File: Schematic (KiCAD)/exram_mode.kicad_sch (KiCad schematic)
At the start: 95 parts

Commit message: - Lots of additional comments and signal name improvements.  - "Don't know what this is yet but it is important" section of the pulse channels:    - I worked out the logic and it is a 4-bit binary up-counter with preload, made from gates and D-latches instead of T-flip-flops.    - It is extremely similar to the envelope counter, but takes twice the die space and much more traces.    - None of its outputs go anywhere else, so I believe that it has no actual function.    - It seems to be a previous attempt at making the envelope counter and it got disconnected and left in.    - Each pulse channel has its own copy and I moved both of them to the "Artifacts" sheet.    - The wasted space amounts to about half of one of the large columns on the left side of the die.  - A couple of "OAI2" cells that noted "unclear order": I determined the correct order of the inputs based on several others which were known.  - Deduced the purpose of the 2 separate methods of scanline detection:    - The one looking for 3 consecutive reads finds the start of a scanline.    - The one counting PPU /RD to find PPU cycle 336, finds the end of the scanline.    - I moved these beside each other on the same sheet for clarity.  - A66.5 Changed from Nand to Nor in order to make sense.  - Basic test mode:    - Pin 92: Active low, enables test mode.    - Pin 29: In test mode, it gives external control of "Scanline Start Detection", which is normally done with the familiar 3 matching PPU reads.  When not in test mode, the pin has no function.    - Pin 30: In test mode, it gives external control of "Scanline End Detection", which is normally done by counting PPU /RD to find PPU cycle 336.  It also gives control of "Pulse Length Clock" when in test mode.  When not in test mode, the pin has no function.    - Pin 98/SL3: In test mode, it gives external control of "Pulse Timer Clock".  Whether or not in test mode, this pin low makes the MMC5 pretend $5104 had not yet been written since reset, probably as a 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
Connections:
- net SL3_PIN is gone; now on net /SL3_PIN_98{PinInv}: BN1. (X)
- net at BL100. (X): now also BL101. (X); no longer BL99. (/Q)
- net /SL3_PIN_98{PinInv}: now reaches BN1. (X)
- net /SL3_PIN_98{PinInv}: no longer BL98. (/Q)
- net at BL90. (X): now also BL91. (X); no longer BL89. (/Q)
- net V-Split_Rendering{N15}: now reaches BK92. (X)
- net V-Split_Rendering{N15}: now also BK94. (X); no longer BK93. (X)
- net at BL93. (X): now also BL92. (X); no longer BN2. (X)
- net at BJ10. (X): now also BJ11. (/Q7); no longer BJ9. (X)
- net at BL88. (X): now also BL86. (X); no longer BL84. (X)
- net at BL92. (X): now also BL94. (X); no longer BL93. (X)
- net at BM9. (X): now also BM10. (X); no longer BM8. (X)
- net at BM10. (X): now also BL91. (X); no longer BM9. (X)
- net at BL84. (X): now also BL85. (X); no longer BL87. (X)
- net at BL103. (X): now also BJ39b. (X); no longer BL95. (X)
- net at BL85. (X): now also BL86. (X); no longer BL82. (X)
- net at BM3. (X): now also BM4. (X); no longer BM2. (X)
- net at BM4. (X): now also BM5. (X); no longer BM3. (X)
- net at BL106. (X): now also BL109. (/Q); no longer BL105. (X)
- removed net V-Split_Side_Latched{N15}: BK92. (X), BK94. (X)
- new net: BL81. (X), BL87. (X)
- new net: BJ40. (Q9), BK78. (Q7), BK89. (X)
- new net: BK84. (X), BL102. (X), BL105. (X), BL107. (X), BN3. (X), BN4. (X)
- new net: BK83. (X), BK84. (X)
- new net: BK84. (X), BK86. (X)
- new net: BL102. (X), BL99. (/Q)
- new net: BL108. (X), BL99. (/Q)
- new net: BL100. (X), BL99. (/Q)
- new net: BL93. (X), BL94. (X), BL98. (/Q)
- new net: BL98. (/Q), BN1. (X)
- new net: BJ40. (Q9), BJ43. (X)
- new net: BK91. (X), BK93. (X)
- new net: BK77. (Q7), BK90. (X)
- new net: BK77. (Q7), BK78. (Q7) (x8)
- new net: BK79. (X), BK81. (X), BK82. (Q1)
- new net: BL89. (/Q), BL90. (X)
- new net: BK92. (X), BK93. (X)
- new net: BL93. (X), BN2. (X)
- new net: BJ7. (X), BJ9. (X)
- new net: BJ10. (X), BJ9. (X)
- new net: BJ32. (X), BJ33. (X), BJ34. (X), BJ35. (X), BJ36. (X), BJ37. (X), BJ38. (X), BJ39. (X), BJ39b. (X) (x2)
- new net: BL84. (X), BL88. (X)
- new net: BL88. (X), BM5. (X), BM6. (X)
- new net: BM8. (X), BM9. (X)
- new net: BK79. (X), BK82. (Q1), BL96. (X)
- new net: BL84. (X), BL87. (X)
- new net: BL104. (X), BL95. (X)
- new net: BL103. (X), BL95. (X)
- new net: BL82. (X), BL85. (X)
- new net: BL83. (X), BL84. (X)
- new net: BJ51. (X), BK96. (X)
- new net: BM2. (X), BM3. (X)
- new net: BK80. (X), BK82. (Q1)
- new net: BL105. (X), BL106. (X)
- new net: BL91. (X), BL92. (X)
- new net: BJ40. (Q9), BJ50. (X)
- new net: BJ40. (Q9), BJ46. (X)
- new net: BJ40. (Q9), BJ42. (X)
- new net: BJ40. (Q9), BJ44. (X)
- new net: BJ40. (Q9), BJ49. (X)
- new net: BJ40. (Q9), BJ45. (X)
- new net: BJ40. (Q9), BJ48. (X)
- new net: BJ40. (Q9), BJ47. (X)
- new net: BJ40. (Q9), BJ41. (X)
- new net: BK94. (X), BK95. (X)
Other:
- note added: "Consider: ExRAM NEVER contains pattern tables and that should be related to how PPU /A13 is being used here."
- note added: "Question: Why should we care about PPU /A13 AT ALL when the CPU has control of ExRAM address bus? Consider: ExRAM can still be used as a nametable when ExRAM mode is set to CPU mode."
- note added: "TRUE when: ExRAM is mode $1x, which gives CPU access but no PPU access, *OR* PPU is accessing NT or AT"
- note added: "That doesn't make sense because what if you have a nametable assigned to ExRAM in $5105? It needs ExRAM Ax coming from PPU. Signal A9 (+ExRAM Nametable Access) is VERY closeby but no obvious connection"
- note added: "This is the write signal for the ExRAM itself."
- note added: "Writing to ExRAM via $5C00-5FFF in mode %10"
- note added: "Writing to an ExRAM nametable via PPU via $2000"
- moved on the sheet: BJ40, BJ41, BJ42, BJ43, BJ44, BJ45, BJ46, BJ47, BJ48, BJ49, BJ50, BJ51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

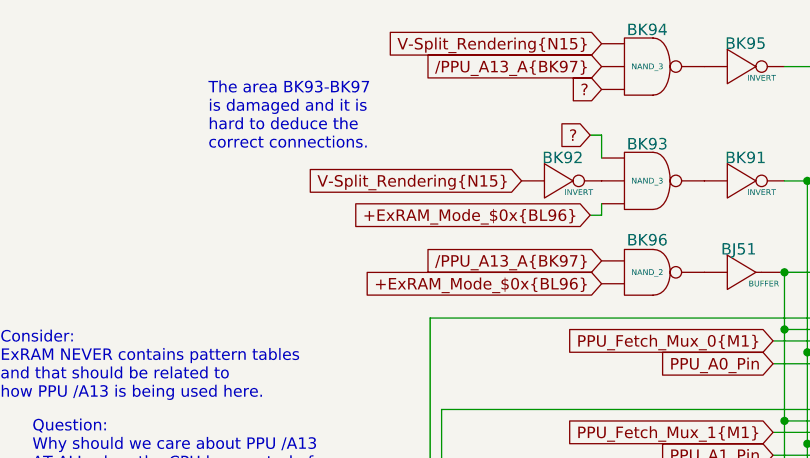
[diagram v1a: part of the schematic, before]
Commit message: - I have fixed all of the problems I was having in the $2006 section, and things are all going places that make sense now.  - I am making good progress on the timer as well.  - I pulled a couple changes back into the letterless SVG and updated the schematic.
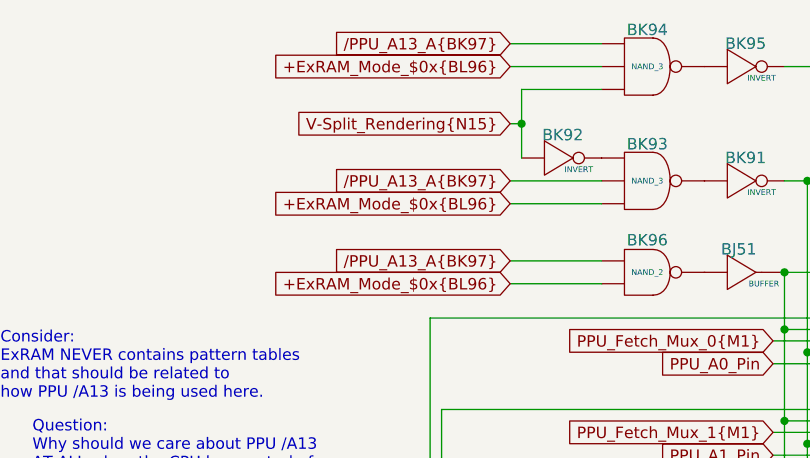
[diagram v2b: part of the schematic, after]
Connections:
- net +ExRAM_Mode_$0x{BL96}: now also BK94. (X)
- net ?: no longer BK93. (X), BK94. (X)
- net /PPU_A13_A{BK97}: now also BK93. (X)
- net at BL100. (X): now also BL101. (X); no longer BL99. (/Q)
- net at BL90. (X): now also BL91. (X); no longer BL89. (/Q)
- net at BL93. (X): now also BL92. (X); no longer BN2. (X)
- net at BJ10. (X): now also BJ11. (/Q7); no longer BJ9. (X)
- net at BL88. (X): now also BL86. (X); no longer BL84. (X)
- net at BL92. (X): now also BL94. (X); no longer BL93. (X)
- net at BM9. (X): now also BM10. (X); no longer BM8. (X)
- net at BM10. (X): now also BL91. (X); no longer BM9. (X)
- net at BL84. (X): now also BL85. (X); no longer BL87. (X)
- net at BL103. (X): now also BJ39b. (X); no longer BL95. (X)
- net at BL85. (X): now also BL86. (X); no longer BL82. (X)
- net at BM3. (X): now also BM4. (X); no longer BM2. (X)
- net at BM4. (X): now also BM5. (X); no longer BM3. (X)
- net at BL106. (X): now also BL109. (/Q); no longer BL105. (X)
- new net: BL81. (X), BL87. (X)
- new net: BJ40. (Q9), BK78. (Q7), BK89. (X)
- new net: BK84. (X), BL102. (X), BL105. (X), BL107. (X), BN3. (X), BN4. (X)
- new net: BK83. (X), BK84. (X)
- new net: BK84. (X), BK86. (X)
- new net: BL102. (X), BL99. (/Q)
- new net: BL108. (X), BL99. (/Q)
- new net: BL100. (X), BL99. (/Q)
- new net: BL93. (X), BL94. (X), BL98. (/Q)
- new net: BL98. (/Q), BN1. (X)
- new net: BJ40. (Q9), BJ43. (X)
- new net: BK91. (X), BK93. (X)
- new net: BK77. (Q7), BK90. (X)
- new net: BK77. (Q7), BK78. (Q7) (x8)
- new net: BK79. (X), BK81. (X), BK82. (Q1)
- new net: BL89. (/Q), BL90. (X)
- new net: BK92. (X), BK93. (X)
- new net: BL93. (X), BN2. (X)
- new net: BJ7. (X), BJ9. (X)
- new net: BJ10. (X), BJ9. (X)
- new net: BJ32. (X), BJ33. (X), BJ34. (X), BJ35. (X), BJ36. (X), BJ37. (X), BJ38. (X), BJ39. (X), BJ39b. (X) (x2)
- new net: BL84. (X), BL88. (X)
- new net: BL88. (X), BM5. (X), BM6. (X)
- new net: BM8. (X), BM9. (X)
- new net: BK79. (X), BK82. (Q1), BL96. (X)
- new net: BL84. (X), BL87. (X)
- new net: BL104. (X), BL95. (X)
- new net: BL103. (X), BL95. (X)
- new net: BL82. (X), BL85. (X)
- new net: BL83. (X), BL84. (X)
- new net: BJ51. (X), BK96. (X)
- new net: BM2. (X), BM3. (X)
- new net: BK80. (X), BK82. (Q1)
- new net: BL105. (X), BL106. (X)
- new net: BL91. (X), BL92. (X)
- new net: BJ40. (Q9), BJ50. (X)
- new net: BJ40. (Q9), BJ46. (X)
- new net: BJ40. (Q9), BJ42. (X)
- new net: BJ40. (Q9), BJ44. (X)
- new net: BJ40. (Q9), BJ49. (X)
- new net: BJ40. (Q9), BJ45. (X)
- new net: BJ40. (Q9), BJ48. (X)
- new net: BJ40. (Q9), BJ47. (X)
- new net: BJ40. (Q9), BJ41. (X)
- new net: BK94. (X), BK95. (X)
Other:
- note removed: "The area BK93-BK97 is damaged and it is hard to deduce the correct connections."
- moved on the sheet: BK92
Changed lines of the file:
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@@
 		)
 	)
-	(text "The area BK93-BK97\nis damaged and it is\nhard to deduce the\ncorrect connections."
-		(exclude_from_sim no)
-		(at 236.982 27.178 0)
-		(effects
-			(font
-				(size 1.27 1.27)
-			)
-			(justify left)
-		)
-	)
 	(text "Writing to ExRAM\nvia $5C00-5FFF\nin mode %10"
 		(exclude_from_sim no)
@@
 	)
 	(junction
+		(at 271.78 27.94)
+		(diameter 0)
+		(color 0 0 0 0)
+	)
+	(junction
 		(at 118.11 76.2)
 		(diameter 0)
@@
 	(wire
 		(pts
+			(xy 270.51 34.29) (xy 280.67 34.29)
+		)
+		(stroke
+			(width 0)
+			(type default)
+		)
+	)
+	(wire
+		(pts
 			(xy 86.36 33.02) (xy 78.74 33.02)
 		)
@@
 	(wire
 		(pts
+			(xy 270.51 43.18) (xy 280.67 43.18)
+		)
+		(stroke
+			(width 0)
+			(type default)
+		)
+	)
+	(wire
+		(pts
 			(xy 66.04 82.55) (xy 66.04 91.44)
 		)
@@
 	(wire
 		(pts
-			(xy 280.67 38.1) (xy 279.4 38.1)
-		)
-		(stroke
-			(width 0)
-			(type default)
-		)
-	)
-	(wire
-		(pts
 			(xy 54.61 222.25) (xy 53.34 222.25)
 		)
@@
 	(wire
 		(pts
-			(xy 279.4 29.21) (xy 280.67 29.21)
-		)
-		(stroke
-			(width 0)
-			(type default)
-		)
-	)
-	(wire
-		(pts
 			(xy 299.72 85.09) (xy 308.61 85.09)
 		)
@@
 	(wire
 		(pts
+			(xy 270.51 21.59) (xy 280.67 21.59)
+		)
+		(stroke
+			(width 0)
+			(type default)
+		)
+	)
+	(wire
+		(pts
 			(xy 303.53 104.14) (xy 303.53 93.98)
 		)
@@
 	(wire
 		(pts
+			(xy 270.51 45.72) (xy 280.67 45.72)
+		)
+		(stroke
+			(width 0)
+			(type default)
+		)
+	)
+	(wire
+		(pts
 			(xy 113.03 124.46) (xy 113.03 132.08)
 		)
@@
 	(wire
 		(pts
+			(xy 270.51 19.05) (xy 280.67 19.05)
+		)
+		(stroke
+			(width 0)
+			(type default)
+		)
+	)
+	(wire
+		(pts
 			(xy 303.53 73.66) (xy 303.53 63.5)
 		)
@@
 	(wire
 		(pts
+			(xy 271.78 27.94) (xy 271.78 24.13)
+		)
+		(stroke
+			(width 0)
+			(type default)
+		)
+	)
+	(wire
+		(pts
 			(xy 128.27 167.64) (xy 128.27 182.88)
 		)
@@
 	(wire
 		(pts
-			(xy 280.67 36.83) (xy 280.67 38.1)
+			(xy 270.51 36.83) (xy 280.67 36.83)
 		)
 		(stroke
@@
 	(wire
 		(pts
-			(xy 118.11 76.2) (xy 127 76.2)
+			(xy 270.51 27.94) (xy 271.78 27.94)
 		)
 		(stroke
@@
 	(wire
 		(pts
-			(xy 100.33 168.91) (xy 97.79 168.91)
+			(xy 118.11 76.2) (xy 127 76.2)
 		)
 		(stroke
@@
 	(wire
 		(pts
-			(xy 243.84 143.51) (xy 243.84 153.67)
+			(xy 100.33 168.91) (xy 97.79 168.91)
 		)
 		(stroke
@@
 	(wire
 		(pts
-			(xy 77.47 81.28) (xy 77.47 83.82)
+			(xy 243.84 143.51) (xy 243.84 153.67)
 		)
 		(stroke
@@
 	(wire
 		(pts
-			(xy 300.99 60.96) (xy 308.61 60.96)
+			(xy 77.47 81.28) (xy 77.47 83.82)
 		)
 		(stroke
@@
 	(wire
 		(pts
-			(xy 262.89 120.65) (xy 260.35 120.65)
+			(xy 300.99 60.96) (xy 308.61 60.96)
 		)
 		(stroke
@@
 	(wire
 		(pts
-			(xy 303.53 134.62) (xy 303.53 124.46)
+			(xy 262.89 120.65) (xy 260.35 120.65)
 		)
 		(stroke
@@
 	(wire
 		(pts
-			(xy 269.24 133.35) (xy 260.35 133.35)
+			(xy 303.53 134.62) (xy 303.53 124.46)
 		)
 		(stroke
@@
 	(wire
 		(pts
-			(xy 280.67 29.21) (xy 280.67 31.75)
+			(xy 269.24 133.35) (xy 260.35 133.35)
 		)
 		(stroke
@@
 	(wire
 		(pts
+			(xy 271.78 27.94) (xy 271.78 31.75)
+		)
+		(stroke
+			(width 0)
+			(type default)
+		)
+	)
+	(wire
+		(pts
 			(xy 271.78 130.81) (xy 271.78 138.43)
 		)
@@
 	(wire
 		(pts
+			(xy 271.78 24.13) (xy 280.67 24.13)
+		)
+		(stroke
+			(width 0)
+			(type default)
+		)
+	)
+	(wire
+		(pts
 			(xy 264.16 123.19) (xy 260.35 123.19)
 		)
@@
 	(global_label "+ExRAM_Mode_$0x{BL96}"
 		(shape input)
-		(at 279.4 38.1 180)
+		(at 270.51 36.83 180)
 		(fields_autoplaced yes)
 		(effects
@@
 		)
 		(property "Intersheetrefs" "${INTERSHEET_REFS}"
-			(at 252.2245 38.1 0)
+			(at 243.3345 36.83 0)
 			(effects
 				(font
@@
 	(global_label "{slash}PPU_A13_A{BK97}"
 		(shape input)
-		(at 280.67 21.59 180)
+		(at 270.51 34.29 180)
+		(fields_autoplaced yes)
+		(effects
+			(font
+				(size 1.27 1.27)
+			)
+			(justify right)
+		)
+		(property "Intersheetrefs" "${INTERSHEET_REFS}"
+			(at 249.14 34.29 0)
+			(effects
+				(font
+					(size 1.27 1.27)
+				)
+				(justify right)
+				(hide yes)
+			)
+		)
+	)
+	(global_label "{slash}PPU_A13_A{BK97}"
+		(shape input)
+		(at 270.51 19.05 180)
 		(fields_autoplaced yes)
 		(effects
@@
 		)
 		(property "Intersheetrefs" "${INTERSHEET_REFS}"
-			(at 259.3 21.59 0)
+			(at 249.14 19.05 0)
 			(effects
 				(font
@@
 	(global_label "+ExRAM_Mode_$0x{BL96}"
 		(shape input)
+		(at 270.51 21.59 180)
+		(fields_autoplaced yes)
+		(effects
+			(font
+				(size 1.27 1.27)
+			)
+			(justify right)
+		)
+		(property "Intersheetrefs" "${INTERSHEET_REFS}"
+			(at 243.3345 21.59 0)
+			(effects
+				(font
+					(size 1.27 1.27)
+				)
+				(justify right)
+				(hide yes)
+			)
+		)
+	)
+	(global_label "+ExRAM_Mode_$0x{BL96}"
+		(shape input)
 		(at 219.71 203.2 180)
 		(fields_autoplaced yes)
@@
 		)
 	)
-	(global_label "V-Split_Rendering{N15}"
-		(shape input)
-		(at 280.67 19.05 180)
-		(fields_autoplaced yes)
-		(effects
-			(font
-				(size 1.27 1.27)
-			)
-			(justify right)
-		)
-		(property "Intersheetrefs" "${INTERSHEET_REFS}"
-			(at 254.8249 19.05 0)
-			(effects
-				(font
-					(size 1.27 1.27)
-				)
-				(justify right)
-				(hide yes)
-			)
-		)
-	)
 	(global_label "+PPU_RD_A{BJ8}"
 		(shape input)
@@
 	(global_label "+ExRAM_Mode_$0x{BL96}"
 		(shape input)
-		(at 280.67 45.72 180)
+		(at 270.51 45.72 180)
 		(fields_autoplaced yes)
 		(effects
@@
 		)
 		(property "Intersheetrefs" "${INTERSHEET_REFS}"
-			(at 253.4945 45.72 0)
+			(at 243.3345 45.72 0)
 			(effects
 				(font
@@
 		)
 	)
-	(global_label "?"
-		(shape input)
-		(at 279.4 29.21 180)
-		(fields_autoplaced yes)
-		(effects
-			(font
-				(size 1.27 1.27)
-			)
-			(justify right)
-		)
-		(property "Intersheetrefs" "${INTERSHEET_REFS}"
-			(at 275.3262 29.21 0)
-			(effects
-				(font
-					(size 1.27 1.27)
-				)
-				(justify right)
-				(hide yes)
-			)
-		)
-	)
 	(global_label "{slash}CPU_Write_To_ExRAM_Any_Mode{BK85}"
 		(shape input)
@@
 	(global_label "V-Split_Rendering{N15}"
 		(shape input)
-		(at 271.78 34.29 180)
+		(at 270.51 27.94 180)
 		(fields_autoplaced yes)
 		(effects
@@
 		)
 		(property "Intersheetrefs" "${INTERSHEET_REFS}"
-			(at 245.9349 34.29 0)
+			(at 244.6649 27.94 0)
 			(effects
 				(font
@@
 		)
 	)
-	(global_label "?"
-		(shape input)
-		(at 280.67 24.13 180)
-		(fields_autoplaced yes)
-		(effects
-			(font
-				(size 1.27 1.27)
-			)
-			(justify right)
-		)
-		(property "Intersheetrefs" "${INTERSHEET_REFS}"
-			(at 276.5962 24.13 0)
-			(effects
-				(font
-					(size 1.27 1.27)
-				)
-				(justify right)
-				(hide yes)
-			)
-		)
-	)
 	(global_label "ExRAM_D2_Read"
 		(shape input)
@@
 	(global_label "{slash}PPU_A13_A{BK97}"
 		(shape input)
-		(at 280.67 43.18 180)
+		(at 270.51 43.18 180)
 		(fields_autoplaced yes)
 		(effects
@@
 		)
 		(property "Intersheetrefs" "${INTERSHEET_REFS}"
-			(at 259.3 43.18 0)
+			(at 249.14 43.18 0)
 			(effects
 				(font
@@
 		(lib_name "INVERT_11")
 		(lib_id "MMC5:INVERT")
-		(at 276.86 34.29 0)
+		(at 276.86 31.75 0)
 		(unit 1)
 		(exclude_from_sim no)
@@
 		(fields_autoplaced yes)
 		(property "Reference" "BK92"
-			(at 276.352 30.988 0)
+			(at 276.352 28.448 0)
 			(do_not_autoplace yes)
 			(effects
@@
 		)
 		(property "Value" "INVERT"
-			(at 278.13 35.56 0)
+			(at 278.13 33.02 0)
 			(do_not_autoplace yes)
 			(effects
@@
 		)
 		(property "Footprint" ""
-			(at 276.86 34.29 0)
+			(at 276.86 31.75 0)
 			(effects
 				(font
@@
 		)
 		(property "Datasheet" ""
-			(at 276.86 34.29 0)
+			(at 276.86 31.75 0)
 			(effects
 				(font
@@
 		)
 		(property "Description" ""
-			(at 276.86 34.29 0)
+			(at 276.86 31.75 0)
 			(effects
 				(font

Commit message: Schematic and SVG Updates
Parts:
- removed BN1: INVERT, symbol MMC5:INVERT
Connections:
- net ? is gone; now on net /Q{BL109}: BL109. (/Q)
- net Q{BL109} is gone; now on net /Q{BL109}: BK89. (X), BL108. (X), BL109. (/Q)
- net /Q{BL109}: now reaches BL108. (X)
- net /Q{BL109}: no longer BL99. (/Q)
- net at BL100. (X): now also BL101. (X); no longer BL99. (/Q)
- net at BL90. (X): now also BL91. (X); no longer BL89. (/Q)
- net at BL93. (X): now also BL92. (X); no longer BN2. (X)
- net at BJ10. (X): now also BJ11. (/Q7); no longer BJ9. (X)
- net at BL88. (X): now also BL86. (X); no longer BL84. (X)
- net at BL92. (X): now also BL94. (X); no longer BL93. (X)
- net at BM9. (X): now also BM10. (X); no longer BM8. (X)
- net at BM10. (X): now also BL91. (X); no longer BM9. (X)
- net at BL84. (X): now also BL85. (X); no longer BL87. (X)
- net at BL103. (X): now also BJ39b. (X); no longer BL95. (X)
- net at BL85. (X): now also BL86. (X); no longer BL82. (X)
- net at BM3. (X): now also BM4. (X); no longer BM2. (X)
- net at BM4. (X): now also BM5. (X); no longer BM3. (X)
- net at BL106. (X): now also BL109. (/Q); no longer BL105. (X)
- new net: BL81. (X), BL87. (X)
- new net: BJ40. (Q9), BK78. (Q7), BK89. (X)
- new net: BK84. (X), BL102. (X), BL105. (X), BL107. (X), BN3. (X), BN4. (X)
- new net: BK83. (X), BK84. (X)
- new net: BK84. (X), BK86. (X)
- new net: BL108. (X), BL99. (/Q)
- new net: BL100. (X), BL99. (/Q)
- new net: BL93. (X), BL94. (X), BL98. (/Q)
- new net: BJ40. (Q9), BJ43. (X)
- new net: BK91. (X), BK93. (X)
- new net: BK77. (Q7), BK90. (X)
- new net: BK77. (Q7), BK78. (Q7) (x8)
- new net: BK79. (X), BK81. (X), BK82. (Q1)
- new net: BL89. (/Q), BL90. (X)
- new net: BK92. (X), BK93. (X)
- new net: BL93. (X), BN2. (X)
- new net: BJ7. (X), BJ9. (X)
- new net: BJ10. (X), BJ9. (X)
- new net: BJ32. (X), BJ33. (X), BJ34. (X), BJ35. (X), BJ36. (X), BJ37. (X), BJ38. (X), BJ39. (X), BJ39b. (X) (x2)
- new net: BL84. (X), BL88. (X)
- new net: BL88. (X), BM5. (X), BM6. (X)
- new net: BM8. (X), BM9. (X)
- new net: BK79. (X), BK82. (Q1), BL96. (X)
- new net: BL84. (X), BL87. (X)
- new net: BL104. (X), BL95. (X)
- new net: BL103. (X), BL95. (X)
- new net: BL82. (X), BL85. (X)
- new net: BL83. (X), BL84. (X)
- new net: BJ51. (X), BK96. (X)
- new net: BM2. (X), BM3. (X)
- new net: BK80. (X), BK82. (Q1)
- new net: BL105. (X), BL106. (X)
- new net: BL91. (X), BL92. (X)
- new net: BJ40. (Q9), BJ50. (X)
- new net: BJ40. (Q9), BJ46. (X)
- new net: BJ40. (Q9), BJ42. (X)
- new net: BJ40. (Q9), BJ44. (X)
- new net: BJ40. (Q9), BJ49. (X)
- new net: BJ40. (Q9), BJ45. (X)
- new net: BJ40. (Q9), BJ48. (X)
- new net: BJ40. (Q9), BJ47. (X)
- new net: BJ40. (Q9), BJ41. (X)
- new net: BK94. (X), BK95. (X)
- new net +Invalid_A0_M2_Sequence{BN1}: BL98. (/Q)
- new net 1: BL109. (/Q)
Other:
- note added: "Appears to go nowhere."
- note added: "MMC5 Only"
- note added: "MMC5A Only"
- note removed: "Appears to go nowhere but maybe goes over BK82 somewhow."
- moved on the sheet: BL102
